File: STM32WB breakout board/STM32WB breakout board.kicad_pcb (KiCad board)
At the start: 2 copper layers, 70 x 80 mm, 37 parts, among them J1 Conn_02x10_Counter_Clockwise, J2 Conn_02x10_Counter_Clockwise, J3 RSP-122811-02, J4 Conn_02x10_Counter_Clockwise, J5 Conn_02x10_Counter_Clockwise, U1 STM32WB15CCU6, X1 32 MHz, X2 32.768 kHz

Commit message: PCB SMPS section inductors updated
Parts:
- moved L3 77.7 mm to (158.1, 94.5), turned to 90 degrees
- moved L2 74.6 mm to (154.8, 93.7), turned to 180 degrees
- moved C11 4.91 mm to (150.0, 100.0)
- moved C8 3.09 mm to (150.0, 103.8)
- moved C10 2.26 mm to (150.0, 101.2)
- moved C7 1.12 mm to (149.3, 107.5)
- moved X1 0.83 mm to (155.7, 98.9)
- moved C9 0.36 mm to (150.0, 102.5)
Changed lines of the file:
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@@
   (net 82 "unconnected-(J5-Pin_20-Pad20)")
   (footprint "Capacitor_SMD:C_0402_1005Metric" (layer "F.Cu")
-    (at 149.95 103.5)
+    (at 149.97 101.24)
     (descr "Capacitor SMD 0402 (1005 Metric), square (rectangular) end terminal, IPC_7351 nominal, (Body size source: IPC-SM-782 page 76, https://www.pcb-3d.com/wordpress/wp-content/uploads/ipc-sm-782a_amendment_1_and_2.pdf), generated with kicad-footprint-generator")
     (tags "capacitor")
@@
   )
   (footprint "Capacitor_THT:CP_Radial_D5.0mm_P2.00mm" (layer "F.Cu")
-    (at 149.39 108.65)
+    (at 149.26 107.54)
     (descr "CP, Radial series, Radial, pin pitch=2.00mm, , diameter=5mm, Electrolytic Capacitor")
     (tags "CP Radial series Radial pin pitch 2.00mm  diameter 5mm Electrolytic Capacitor")
@@
   )
   (footprint "Capacitor_SMD:C_0402_1005Metric" (layer "F.Cu")
-    (at 149.96 104.9)
+    (at 149.97 99.99)
     (descr "Capacitor SMD 0402 (1005 Metric), square (rectangular) end terminal, IPC_7351 nominal, (Body size source: IPC-SM-782 page 76, https://www.pcb-3d.com/wordpress/wp-content/uploads/ipc-sm-782a_amendment_1_and_2.pdf), generated with kicad-footprint-generator")
     (tags "capacitor")
@@
   )
   (footprint "Crystal:Crystal_SMD_2016-4Pin_2.0x1.6mm" (layer "F.Cu")
-    (at 155.21 98.21 180)
+    (at 155.71 98.87 180)
     (descr "SMD Crystal SERIES SMD2016/4 http://www.q-crystal.com/upload/5/2015552223166229.pdf, 2.0x1.6mm^2 package")
     (tags "SMD SMT crystal")
@@
   )
   (footprint "Capacitor_SMD:C_0402_1005Metric" (layer "F.Cu")
-    (at 149.97 100.73)
+    (at 149.98 103.82)
     (descr "Capacitor SMD 0402 (1005 Metric), square (rectangular) end terminal, IPC_7351 nominal, (Body size source: IPC-SM-782 page 76, https://www.pcb-3d.com/wordpress/wp-content/uploads/ipc-sm-782a_amendment_1_and_2.pdf), generated with kicad-footprint-generator")
     (tags "capacitor")
@@
   )
   (footprint "LQG15WZ10NJ02D:INDC1006X60N" (layer "F.Cu")
-    (at 214.27 48.643)
+    (at 154.77 93.67 180)
     (property "Availability" "In Stock")
     (property "Check_prices" "https://www.snapeda.com/parts/LQG15WZ10NJ02D/Murata+Electronics+North+America/view-part/?ref=eda")
@@
     (property "SnapEDA_Link" "https://www.snapeda.com/parts/LQG15WZ10NJ02D/Murata+Electronics+North+America/view-part/?ref=snap")
     (attr smd)
-    (fp_text reference "L2" (at 0.3 -0.93) (layer "F.SilkS")
+    (fp_text reference "L2" (at 0.01 0.92) (layer "F.SilkS")
         (effects (font (size 0.393701 0.393701) (thickness 0.15)))
     )
@@
     (fp_circle (center 1.2 0) (end 1.3 0)
       (stroke (width 0.2) (type solid)) (fill none) (layer "F.Fab"))
-    (pad "1" smd rect (at -0.468 0) (size 0.46 0.7) (layers "F.Cu" "F.Paste" "F.Mask")
+    (pad "1" smd rect (at -0.468 0 180) (size 0.46 0.7) (layers "F.Cu" "F.Paste" "F.Mask")
       (net 41 "Net-(L2-Pad1)") (pintype "passive") (solder_mask_margin 0.102))
-    (pad "2" smd rect (at 0.468 0) (size 0.46 0.7) (layers "F.Cu" "F.Paste" "F.Mask")
+    (pad "2" smd rect (at 0.468 0 180) (size 0.46 0.7) (layers "F.Cu" "F.Paste" "F.Mask")
       (net 38 "/RF & Power/VLXSMPS") (pintype "passive") (solder_mask_margin 0.102))
   )
@@
   )
   (footprint "Capacitor_SMD:C_0402_1005Metric" (layer "F.Cu")
-    (at 149.95 102.14)
+    (at 149.98 102.5)
     (descr "Capacitor SMD 0402 (1005 Metric), square (rectangular) end terminal, IPC_7351 nominal, (Body size source: IPC-SM-782 page 76, https://www.pcb-3d.com/wordpress/wp-content/uploads/ipc-sm-782a_amendment_1_and_2.pdf), generated with kicad-footprint-generator")
     (tags "capacitor")
@@
   )
   (footprint "LQM21FN100M70L:INDC2012X145N" (layer "F.Cu")
-    (at 220.512 48.26)
+    (at 158.08 94.54 90)
     (property "Availability" "In Stock")
     (property "Check_prices" "https://www.snapeda.com/parts/LQM21FN100M70L/Murata+Electronics+North+America/view-part/?ref=eda")
@@
     (property "SnapEDA_Link" "https://www.snapeda.com/parts/LQM21FN100M70L/Murata+Electronics+North+America/view-part/?ref=snap")
     (attr smd)
-    (fp_text reference "L3" (at -0.46 -1.32) (layer "F.SilkS")
+    (fp_text reference "L3" (at 2.04 -0.01 180) (layer "F.SilkS")
         (effects (font (size 0.393701 0.393701) (thickness 0.15)))
     )
-    (fp_text value "LQM21FN100M70L" (at 1.54 1.32) (layer "F.Fab")
+    (fp_text value "LQM21FN100M70L" (at 1.54 1.32 90) (layer "F.Fab")
         (effects (font (size 0.393701 0.393701) (thickness 0.15)))
     )
@@
     (fp_line (start 1.1 0.72) (end 1.1 -0.72)
       (stroke (width 0.127) (type solid)) (layer "F.Fab"))
-    (pad "1" smd rect (at -0.86 0) (size 1.2 1.47) (layers "F.Cu" "F.Paste" "F.Mask")
+    (pad "1" smd rect (at -0.86 0 90) (size 1.2 1.47) (layers "F.Cu" "F.Paste" "F.Mask")
       (net 36 "/RF & Power/VFBSMPS") (pintype "passive") (solder_mask_margin 0.102))
-    (pad "2" smd rect (at 0.86 0) (size 1.2 1.47) (layers "F.Cu" "F.Paste" "F.Mask")
+    (pad "2" smd rect (at 0.86 0 90) (size 1.2 1.47) (layers "F.Cu" "F.Paste" "F.Mask")
       (net 41 "Net-(L2-Pad1)") (pintype "passive") (solder_mask_margin 0.102))
   )

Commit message: PCB SMPS section inductors updated
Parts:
- moved R2 67.1 mm to (142.8, 93.6), turned to 90 degrees
- moved C5 2.83 mm to (140.1, 92.0)
- moved C6 2.83 mm to (140.1, 94.2)
- moved X2 2.83 mm to (138.2, 93.0)
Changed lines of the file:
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@@
   )
   (footprint "Capacitor_SMD:C_0402_1005Metric" (layer "F.Cu")
-    (at 142.92 92.15 90)
+    (at 140.1 91.96 90)
     (descr "Capacitor SMD 0402 (1005 Metric), square (rectangular) end terminal, IPC_7351 nominal, (Body size source: IPC-SM-782 page 76, https://www.pcb-3d.com/wordpress/wp-content/uploads/ipc-sm-782a_amendment_1_and_2.pdf), generated with kicad-footprint-generator")
     (tags "capacitor")
@@
   )
   (footprint "Crystal:Crystal_SMD_2012-2Pin_2.0x1.2mm" (layer "F.Cu")
-    (at 141.01 93.2 90)
+    (at 138.19 93.01 90)
     (descr "SMD Crystal 2012/2 http://txccrystal.com/images/pdf/9ht11.pdf, 2.0x1.2mm^2 package")
     (tags "SMD SMT crystal")
@@
   )
   (footprint "Capacitor_SMD:C_0402_1005Metric" (layer "F.Cu")
-    (at 142.92 94.38 -90)
+    (at 140.1 94.19 -90)
     (descr "Capacitor SMD 0402 (1005 Metric), square (rectangular) end terminal, IPC_7351 nominal, (Body size source: IPC-SM-782 page 76, https://www.pcb-3d.com/wordpress/wp-content/uploads/ipc-sm-782a_amendment_1_and_2.pdf), generated with kicad-footprint-generator")
     (tags "capacitor")
@@
   )
   (footprint "Resistor_SMD:R_1206_3216Metric" (layer "F.Cu")
-    (at 146.66 26.6)
+    (at 142.8 93.5675 90)
     (descr "Resistor SMD 1206 (3216 Metric), square (rectangular) end terminal, IPC_7351 nominal, (Body size source: IPC-SM-782 page 72, https://www.pcb-3d.com/wordpress/wp-content/uploads/ipc-sm-782a_amendment_1_and_2.pdf), generated with kicad-footprint-generator")
     (tags "resistor")
@@
     (property "ki_keywords" "R res resistor")
     (attr smd)
-    (fp_text reference "R2" (at 0 -1.82) (layer "F.SilkS")
-        (effects (font (size 1 1) (thickness 0.15)))
-    )
-    (fp_text value "10k" (at 0 1.82) (layer "F.Fab")
-        (effects (font (size 1 1) (thickness 0.15)))
-    )
-    (fp_text user "${REFERENCE}" (at 0 0) (layer "F.Fab")
+    (fp_text reference "R2" (at -3.0725 -0.02 180) (layer "F.SilkS")
+        (effects (font (size 1 1) (thickness 0.15)))
+    )
+    (fp_text value "10k" (at 0 1.82 90) (layer "F.Fab")
+        (effects (font (size 1 1) (thickness 0.15)))
+    )
+    (fp_text user "${REFERENCE}" (at 0 0 90) (layer "F.Fab")
         (effects (font (size 0.8 0.8) (thickness 0.12)))
     )
@@
     (fp_line (start 1.6 0.8) (end -1.6 0.8)
       (stroke (width 0.1) (type solid)) (layer "F.Fab"))
-    (pad "1" smd roundrect (at -1.4625 0) (size 1.125 1.75) (layers "F.Cu" "F.Paste" "F.Mask") (roundrect_rratio 0.222222)
+    (pad "1" smd roundrect (at -1.4625 0 90) (size 1.125 1.75) (layers "F.Cu" "F.Paste" "F.Mask") (roundrect_rratio 0.222222)
       (net 26 "GND") (pintype "passive"))
-    (pad "2" smd roundrect (at 1.4625 0) (size 1.125 1.75) (layers "F.Cu" "F.Paste" "F.Mask") (roundrect_rratio 0.222222)
+    (pad "2" smd roundrect (at 1.4625 0 90) (size 1.125 1.75) (layers "F.Cu" "F.Paste" "F.Mask") (roundrect_rratio 0.222222)
       (net 3 "/BOOT0") (pintype "passive"))
     (model "${KICAD6_3DMODEL_DIR}/Resistor_SMD.3dshapes/R_1206_3216Metric.wrl"

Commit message: USB excluded
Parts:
- moved C7 0.31 mm to (149.1, 107.3)
- moved C10 0.14 mm to (150.0, 101.1)
- moved C11 0.14 mm to (150.0, 99.8)
- moved C9 0.14 mm to (150.0, 102.4)
- moved C8 0.14 mm to (150.0, 103.7)
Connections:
- net /USB_N renamed /PA11
- net /USB_P renamed /PA12
- U1 pad 22: /VSSRF -> GND
- U1 pad 32: /VSSSMPS -> GND
- U1 pad 40: /VDDUSB -> 3V3

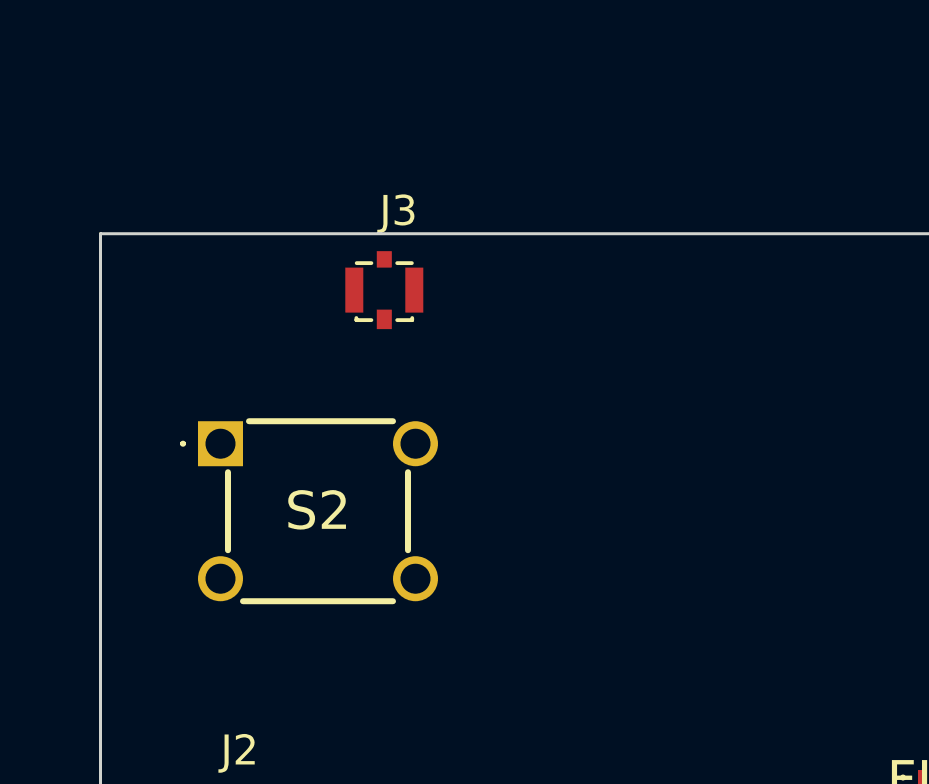
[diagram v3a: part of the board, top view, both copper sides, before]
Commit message: PCB SMPS section inductors updated
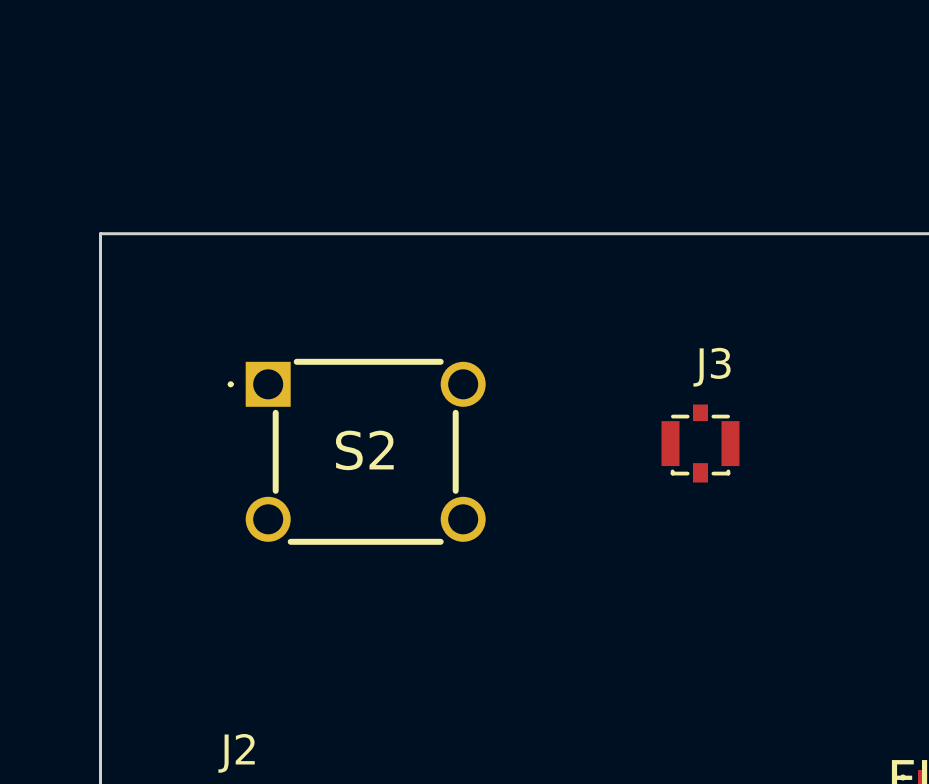
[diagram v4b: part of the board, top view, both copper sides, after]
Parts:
- moved J3 11.7 mm to (134.0, 61.0)
- moved S2 2.54 mm to (119.6, 59.0)
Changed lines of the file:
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@@
   )
   (footprint "RSP-122811-02:SAMTEC_RSP-122811-02" (layer "F.Cu")
-    (at 123.46 55.88)
+    (at 134 60.995)
     (property "Availability" "In Stock")
     (property "Check_prices" "https://www.snapeda.com/parts/RSP-122811-02/Samtec+Inc./view-part/?ref=eda")
@@
   )
   (footprint "Button_Switch_THT:TS026670BK160LCRD" (layer "F.Cu")
-    (at 118 61)
+    (at 119.59 59.02)
     (descr "TS02-66-70-BK-160-LCR-D-2")
     (tags "Switch")

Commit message: PCB button updated
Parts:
- moved R3 40.3 mm to (177.3, 67.5), turned to 90 degrees
- moved R1 35.9 mm to (168.4, 60.2), turned to -90 degrees
- moved C17 30.9 mm to (174.4, 66.9), turned to -90 degrees
- moved S1 8.18 mm to (179.2, 62.8), turned to 180 degrees
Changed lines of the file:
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@@
   )
   (footprint "Button_Switch_THT:TS026670BK160LCRD" (layer "F.Cu")
-    (at 172 59)
+    (at 179.24 62.8 180)
     (descr "TS02-66-70-BK-160-LCR-D-2")
     (tags "Switch")
@@
     (fp_line (start 6.25 5.25) (end 0.25 5.25)
       (stroke (width 0.1) (type solid)) (layer "F.Fab"))
-    (pad "1" thru_hole rect (at 0 0) (size 1.5 1.5) (drill 1) (layers "*.Cu" "*.Mask")
+    (pad "1" thru_hole rect (at 0 0 180) (size 1.5 1.5) (drill 1) (layers "*.Cu" "*.Mask")
       (net 39 "unconnected-(S1-NO_1-Pad1)") (pinfunction "NO_1") (pintype "passive+no_connect"))
-    (pad "2" thru_hole circle (at 6.5 0) (size 1.5 1.5) (drill 1) (layers "*.Cu" "*.Mask")
+    (pad "2" thru_hole circle (at 6.5 0 180) (size 1.5 1.5) (drill 1) (layers "*.Cu" "*.Mask")
       (net 44 "Net-(S1-NO_2)") (pinfunction "NO_2") (pintype "passive"))
-    (pad "3" thru_hole circle (at 0 4.5) (size 1.5 1.5) (drill 1) (layers "*.Cu" "*.Mask")
+    (pad "3" thru_hole circle (at 0 4.5 180) (size 1.5 1.5) (drill 1) (layers "*.Cu" "*.Mask")
       (net 40 "unconnected-(S1-COM_1-Pad3)") (pinfunction "COM_1") (pintype "passive+no_connect"))
-    (pad "4" thru_hole circle (at 6.5 4.5) (size 1.5 1.5) (drill 1) (layers "*.Cu" "*.Mask")
+    (pad "4" thru_hole circle (at 6.5 4.5 180) (size 1.5 1.5) (drill 1) (layers "*.Cu" "*.Mask")
       (net 43 "/USR_BTN") (pinfunction "COM_2") (pintype "passive"))
     (model "TS02-66-70-BK-160-LCR-D.stp"
@@
   )
   (footprint "Resistor_SMD:R_1206_3216Metric" (layer "F.Cu")
-    (at 196.4375 32)
+    (at 177.29 67.4725 90)
     (descr "Resistor SMD 1206 (3216 Metric), square (rectangular) end terminal, IPC_7351 nominal, (Body size source: IPC-SM-782 page 72, https://www.pcb-3d.com/wordpress/wp-content/uploads/ipc-sm-782a_amendment_1_and_2.pdf), generated with kicad-footprint-generator")
     (tags "resistor")
@@
     (property "ki_keywords" "R res resistor")
     (attr smd)
-    (fp_text reference "R3" (at 0 -1.82) (layer "F.SilkS")
-        (effects (font (size 1 1) (thickness 0.15)))
-    )
-    (fp_text value "100k" (at 0 1.82) (layer "F.Fab")
-        (effects (font (size 1 1) (thickness 0.15)))
-    )
-    (fp_text user "${REFERENCE}" (at 0 0) (layer "F.Fab")
+    (fp_text reference "R3" (at -0.06 2.2125 180) (layer "F.SilkS")
+        (effects (font (size 1 1) (thickness 0.15)))
+    )
+    (fp_text value "100k" (at 0 1.82 90) (layer "F.Fab")
+        (effects (font (size 1 1) (thickness 0.15)))
+    )
+    (fp_text user "${REFERENCE}" (at 0 0 90) (layer "F.Fab")
         (effects (font (size 0.8 0.8) (thickness 0.12)))
     )
@@
     (fp_line (start 1.6 0.8) (end -1.6 0.8)
       (stroke (width 0.1) (type solid)) (layer "F.Fab"))
-    (pad "1" smd roundrect (at -1.4625 0) (size 1.125 1.75) (layers "F.Cu" "F.Paste" "F.Mask") (roundrect_rratio 0.222222)
+    (pad "1" smd roundrect (at -1.4625 0 90) (size 1.125 1.75) (layers "F.Cu" "F.Paste" "F.Mask") (roundrect_rratio 0.222222)
       (net 26 "GND") (pintype "passive"))
-    (pad "2" smd roundrect (at 1.4625 0) (size 1.125 1.75) (layers "F.Cu" "F.Paste" "F.Mask") (roundrect_rratio 0.222222)
+    (pad "2" smd roundrect (at 1.4625 0 90) (size 1.125 1.75) (layers "F.Cu" "F.Paste" "F.Mask") (roundrect_rratio 0.222222)
       (net 43 "/USR_BTN") (pintype "passive"))
     (model "${KICAD6_3DMODEL_DIR}/Resistor_SMD.3dshapes/R_1206_3216Metric.wrl"
@@
   )
   (footprint "Capacitor_SMD:C_0402_1005Metric" (layer "F.Cu")
-    (at 194 43)
+    (at 174.43 66.91 -90)
     (descr "Capacitor SMD 0402 (1005 Metric), square (rectangular) end terminal, IPC_7351 nominal, (Body size source: IPC-SM-782 page 76, https://www.pcb-3d.com/wordpress/wp-content/uploads/ipc-sm-782a_amendment_1_and_2.pdf), generated with kicad-footprint-generator")
     (tags "capacitor")
@@
     (property "ki_keywords" "cap capacitor")
     (attr smd)
-    (fp_text reference "C17" (at 0 -1.16) (layer "F.SilkS")
-        (effects (font (size 1 1) (thickness 0.15)))
-    )
-    (fp_text value "100nF" (at 0 1.16) (layer "F.Fab")
-        (effects (font (size 1 1) (thickness 0.15)))
-    )
-    (fp_text user "${REFERENCE}" (at 0 0) (layer "F.Fab")
+    (fp_text reference "C17" (at 1.7 -0.01 -180) (layer "F.SilkS")
+        (effects (font (size 1 1) (thickness 0.15)))
+    )
+    (fp_text value "100nF" (at 0 1.16 90) (layer "F.Fab")
+        (effects (font (size 1 1) (thickness 0.15)))
+    )
+    (fp_text user "${REFERENCE}" (at 0 0 90) (layer "F.Fab")
         (effects (font (size 0.25 0.25) (thickness 0.04)))
     )
@@
     (fp_line (start 0.5 0.25) (end -0.5 0.25)
       (stroke (width 0.1) (type solid)) (layer "F.Fab"))
-    (pad "1" smd roundrect (at -0.48 0) (size 0.56 0.62) (layers "F.Cu" "F.Paste" "F.Mask") (roundrect_rratio 0.25)
+    (pad "1" smd roundrect (at -0.48 0 270) (size 0.56 0.62) (layers "F.Cu" "F.Paste" "F.Mask") (roundrect_rratio 0.25)
       (net 43 "/USR_BTN") (pintype "passive"))
-    (pad "2" smd roundrect (at 0.48 0) (size 0.56 0.62) (layers "F.Cu" "F.Paste" "F.Mask") (roundrect_rratio 0.25)
+    (pad "2" smd roundrect (at 0.48 0 270) (size 0.56 0.62) (layers "F.Cu" "F.Paste" "F.Mask") (roundrect_rratio 0.25)
       (net 26 "GND") (pintype "passive"))
     (model "${KICAD6_3DMODEL_DIR}/Capacitor_SMD.3dshapes/C_0402_1005Metric.wrl"
@@
   )
   (footprint "Resistor_SMD:R_1206_3216Metric" (layer "F.Cu")
-    (at 190.5475 32)
+    (at 168.38 60.2025 -90)
     (descr "Resistor SMD 1206 (3216 Metric), square (rectangular) end terminal, IPC_7351 nominal, (Body size source: IPC-SM-782 page 72, https://www.pcb-3d.com/wordpress/wp-content/uploads/ipc-sm-782a_amendment_1_and_2.pdf), generated with kicad-footprint-generator")
     (tags "resistor")
@@
     (property "ki_keywords" "R res resistor")
     (attr smd)
-    (fp_text reference "R1" (at 0 -1.82) (layer "F.SilkS")
-        (effects (font (size 1 1) (thickness 0.15)))
-    )
-    (fp_text value "1k" (at 0 1.82) (layer "F.Fab")
-        (effects (font (size 1 1) (thickness 0.15)))
-    )
-    (fp_text user "${REFERENCE}" (at 0 0) (layer "F.Fab")
+    (fp_text reference "R1" (at -0.0025 1.86 90) (layer "F.SilkS")
+        (effects (font (size 1 1) (thickness 0.15)))
+    )
+    (fp_text value "1k" (at 0 1.82 90) (layer "F.Fab")
+        (effects (font (size 1 1) (thickness 0.15)))
+    )
+    (fp_text user "${REFERENCE}" (at 0 0 90) (layer "F.Fab")
         (effects (font (size 0.8 0.8) (thickness 0.12)))
     )
@@
     (fp_line (start 1.6 0.8) (end -1.6 0.8)
       (stroke (width 0.1) (type solid)) (layer "F.Fab"))
-    (pad "1" smd roundrect (at -1.4625 0) (size 1.125 1.75) (layers "F.Cu" "F.Paste" "F.Mask") (roundrect_rratio 0.222222)
+    (pad "1" smd roundrect (at -1.4625 0 270) (size 1.125 1.75) (layers "F.Cu" "F.Paste" "F.Mask") (roundrect_rratio 0.222222)
       (net 44 "Net-(S1-NO_2)") (pintype "passive"))
-    (pad "2" smd roundrect (at 1.4625 0) (size 1.125 1.75) (layers "F.Cu" "F.Paste" "F.Mask") (roundrect_rratio 0.222222)
+    (pad "2" smd roundrect (at 1.4625 0 270) (size 1.125 1.75) (layers "F.Cu" "F.Paste" "F.Mask") (roundrect_rratio 0.222222)
       (net 27 "3V3") (pintype "passive"))
     (model "${KICAD6_3DMODEL_DIR}/Resistor_SMD.3dshapes/R_1206_3216Metric.wrl"
